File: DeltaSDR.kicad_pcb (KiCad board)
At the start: 2 copper layers, 100 x 80 mm, 174 parts, among them J1 Conn_01x03_Male, J2 Conn_01x05_Male, J3 Barrel_Jack, J4 USB_A, J5 Conn_Coaxial, Q1 BSS123, Q2 BSS123, Q3 BSS123, Q4 BSS123, Q5 BSS123, Q6 BSS123, T1 Transformer_1P_SS, T2 Transformer_1P_SS, U1 TC1262-33, U10 TLV2464CD, U11 SN74CBT3253, U12 MMG3H21NT1, U2 Si570, U3 SN74CBT3253, U4 PCM3060, U5 CY8C3246PVI-147, U6 TC1262-5, U7 TC1262-5, U8 74HC74, U9 LT6231CSB, Y1 Crystal_GND24

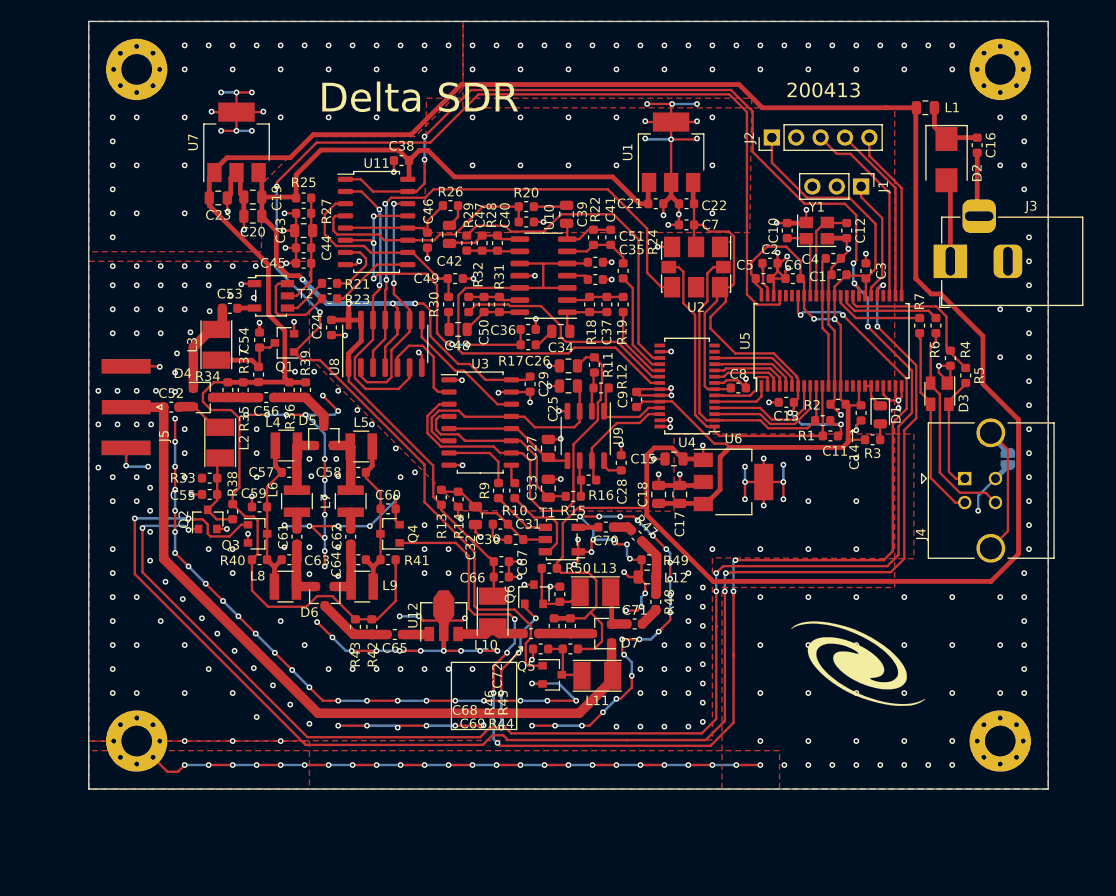
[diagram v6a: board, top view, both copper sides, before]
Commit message: ERC, DRC done, added output for ATU and AMP
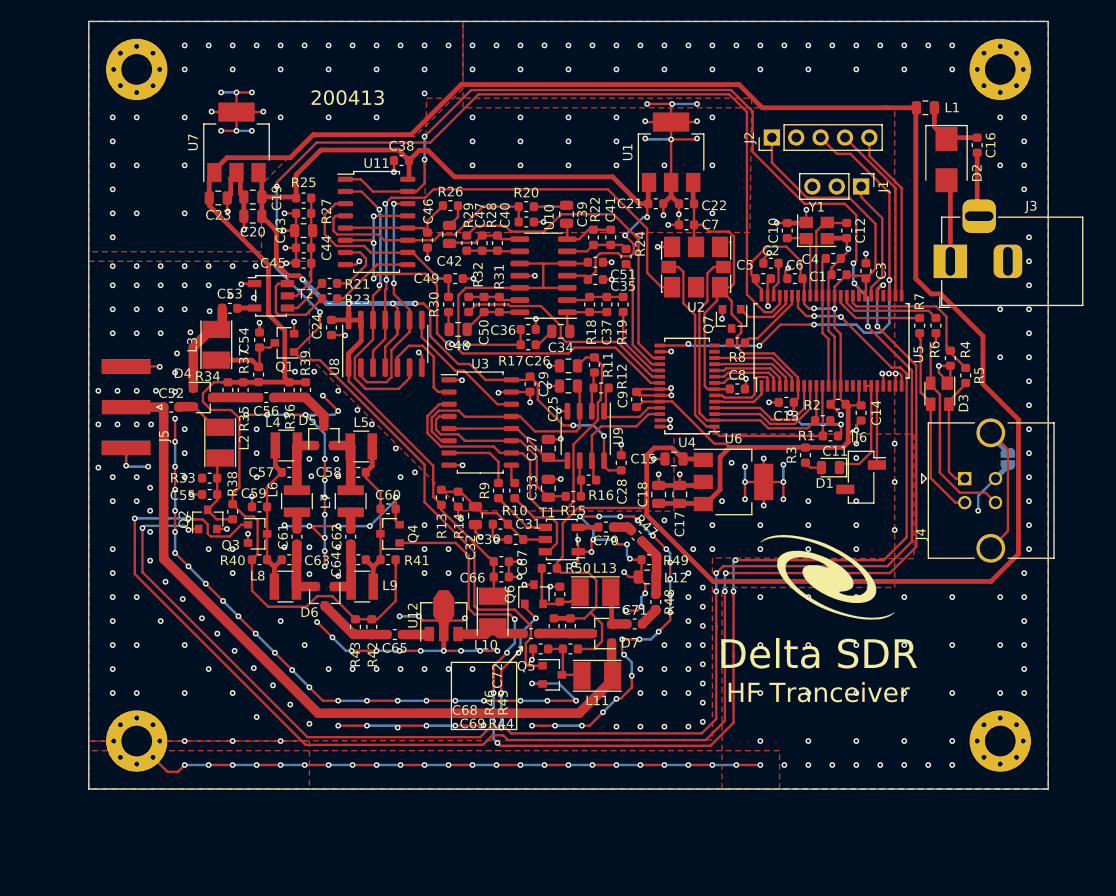
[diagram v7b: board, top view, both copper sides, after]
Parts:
- added J6: Conn_01x02_Male, Connector_PinSocket_2.54mm:PinSocket_1x02_P2.54mm_Vertical_SMD_Pin1Right, F.Cu at (190.5, 107.5)
- added Q7: MMBT3904, Package_TO_SOT_SMD:SOT-23, F.Cu at (177.0, 91.0)
- added R8: 1K, Resistor_SMD:R_0603_1608Metric, F.Cu at (177.6, 93.5)
- moved G*** 9.55 mm to (187.0, 118.0)
- moved D1 7.57 mm to (187.3, 106.5), turned to 180 degrees
- moved R3 7.18 mm to (184.7, 105.2), turned to 90 degrees
- moved R24 1.53 mm to (166.0, 84.5)
- moved C6 0.20 mm to (183.6, 86.8)
- moved C8 0.14 mm to (177.6, 98.3)
- moved C2 0.10 mm to (181.1, 85.2), turned to 180 degrees
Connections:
- net RF_BIT renamed Net-(R33-Pad2)
- C28 pad 1: Net-(C28-Pad1) -> +5V
- C35 pad 1: Net-(C35-Pad1) -> +5V
- U10 pad 4: Net-(C35-Pad1) -> +5V
- U4 pad 15: RESET -> RES
- U5 pad 46: GND -> Net-(C2-Pad1)
- U5 pad 47: Net-(C2-Pad1) -> GND
- U9 pad 8: Net-(C28-Pad1) -> +5V
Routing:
- net +5V: track 142.9 -> 175.2 mm, vias 4 -> 8
- net RES: track 20.3 -> 50.6 mm, vias 0 -> 4
- net Net-(D1-Pad1): track 3.10 -> 11.5 mm
- net AMP: track 0.00 -> 8.25 mm
- net ATU_0: track 0.00 -> 7.44 mm
- net ATU_1: track 0.00 -> 6.45 mm
- net GND: track 531.7 -> 526.8 mm, vias 491 -> 510
- net Net-(C28-Pad1): track 2.52 -> 0.00 mm
- net +5VD: track 106.1 -> 103.6 mm
- net Net-(C35-Pad1): track 2.22 -> 0.00 mm
- net +3V3: track 61.1 -> 59.6 mm
- net +12V: track 304.6 -> 303.2 mm, vias 1 -> 0
- net VOUTR+: track 11.0 -> 12.4 mm
- net VINR: track 12.1 -> 12.8 mm
- net Net-(C25-Pad2): track 24.2 -> 24.9 mm
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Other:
- board text added: "HF Tranceiver"

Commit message: Changed LO position and OPAMPs wiring
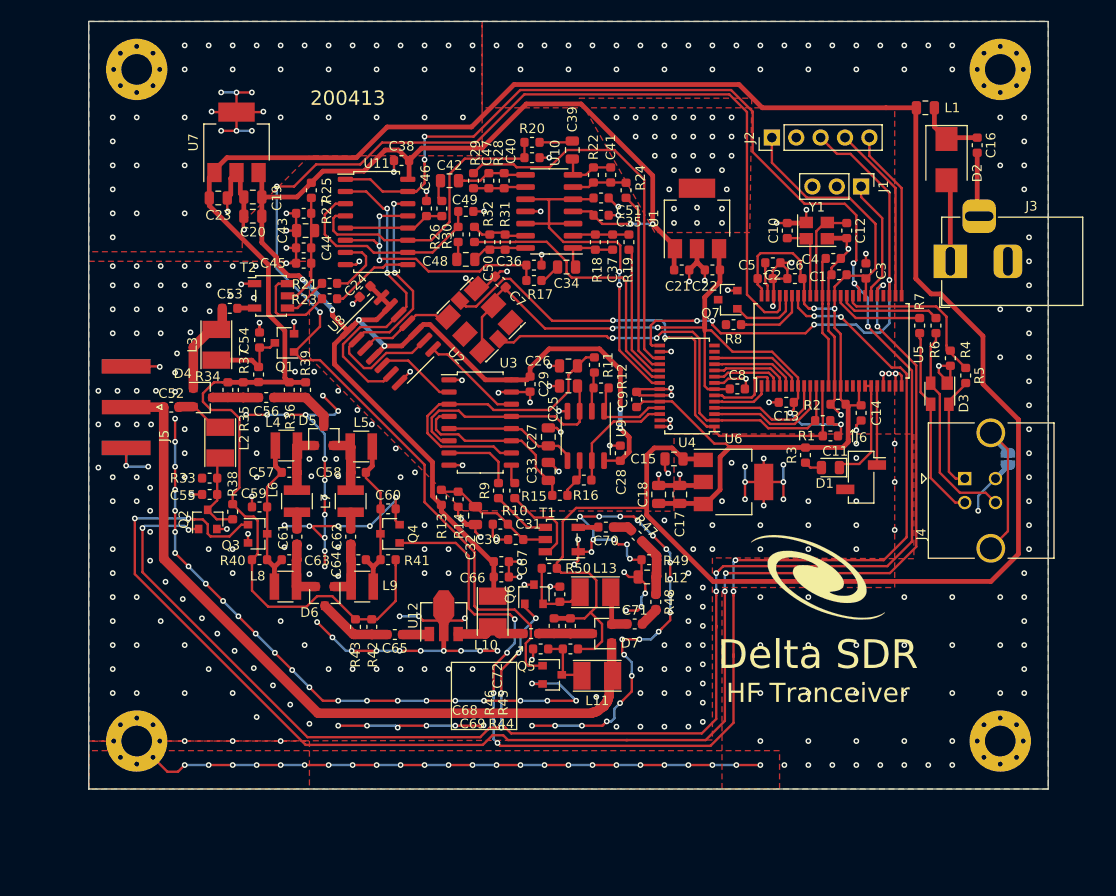
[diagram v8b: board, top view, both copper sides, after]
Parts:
- moved U2 23.3 mm to (150.7, 91.1), turned to 135 degrees
- moved C7 20.3 mm to (152.9, 87.2), turned to 135 degrees
- moved C21 7.41 mm to (171.8, 85.9)
- moved C22 7.41 mm to (175.0, 85.9)
- moved U1 7.41 mm to (173.4, 80.5)
- moved R30 7.37 mm to (148.5, 82.2)
- moved C48 7.34 mm to (149.3, 84.8)
- moved R32 7.32 mm to (150.2, 82.2)
- moved C49 7.09 mm to (149.3, 79.8)
- moved R24 6.90 mm to (166.0, 77.6)
- moved C34 6.73 mm to (159.8, 85.6)
- moved C35 6.73 mm to (163.4, 80.2)
- moved C40 6.73 mm to (156.2, 74.2)
- moved R17 6.73 mm to (156.4, 87.0)
- moved R20 6.73 mm to (156.2, 72.6)
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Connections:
- net Net-(R33-Pad2) renamed RF_BIT
- U5 pad 46: Net-(C2-Pad1) -> GND
- U5 pad 47: GND -> Net-(C2-Pad1)
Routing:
- net Net-(U2-Pad4): track 55.1 -> 10.2 mm, vias 2 -> 0
- net SCL: track 36.9 -> 57.0 mm, vias 0 -> 2
- net GND: track 526.8 -> 511.2 mm, vias 510 -> 516
- net +3V3: track 59.6 -> 72.7 mm, vias 2 -> 4
- net SDA: track 33.6 -> 46.5 mm, vias 0 -> 2
- net Net-(C26-Pad2): track 44.7 -> 32.8 mm
- net VCOM: track 50.0 -> 39.9 mm, vias 0 -> 2
- net +5V: track 175.2 -> 183.2 mm
- net Net-(C36-Pad1): track 36.3 -> 29.1 mm, vias 5 -> 3
- net VOUTR+: track 12.4 -> 19.3 mm
- net QSE_Q: track 25.5 -> 31.9 mm
- net VOUTL-: track 8.13 -> 14.4 mm
- net VOUTL+: track 24.0 -> 30.0 mm
- net VOUTR-: track 34.1 -> 40.0 mm
- net Net-(C40-Pad1): track 25.4 -> 31.1 mm
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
